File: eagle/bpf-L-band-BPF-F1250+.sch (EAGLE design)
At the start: 3 parts, among them U1 BPF-F1250+, X1 SMA-142-0701-801/806, X2 SMA-142-0701-801/806

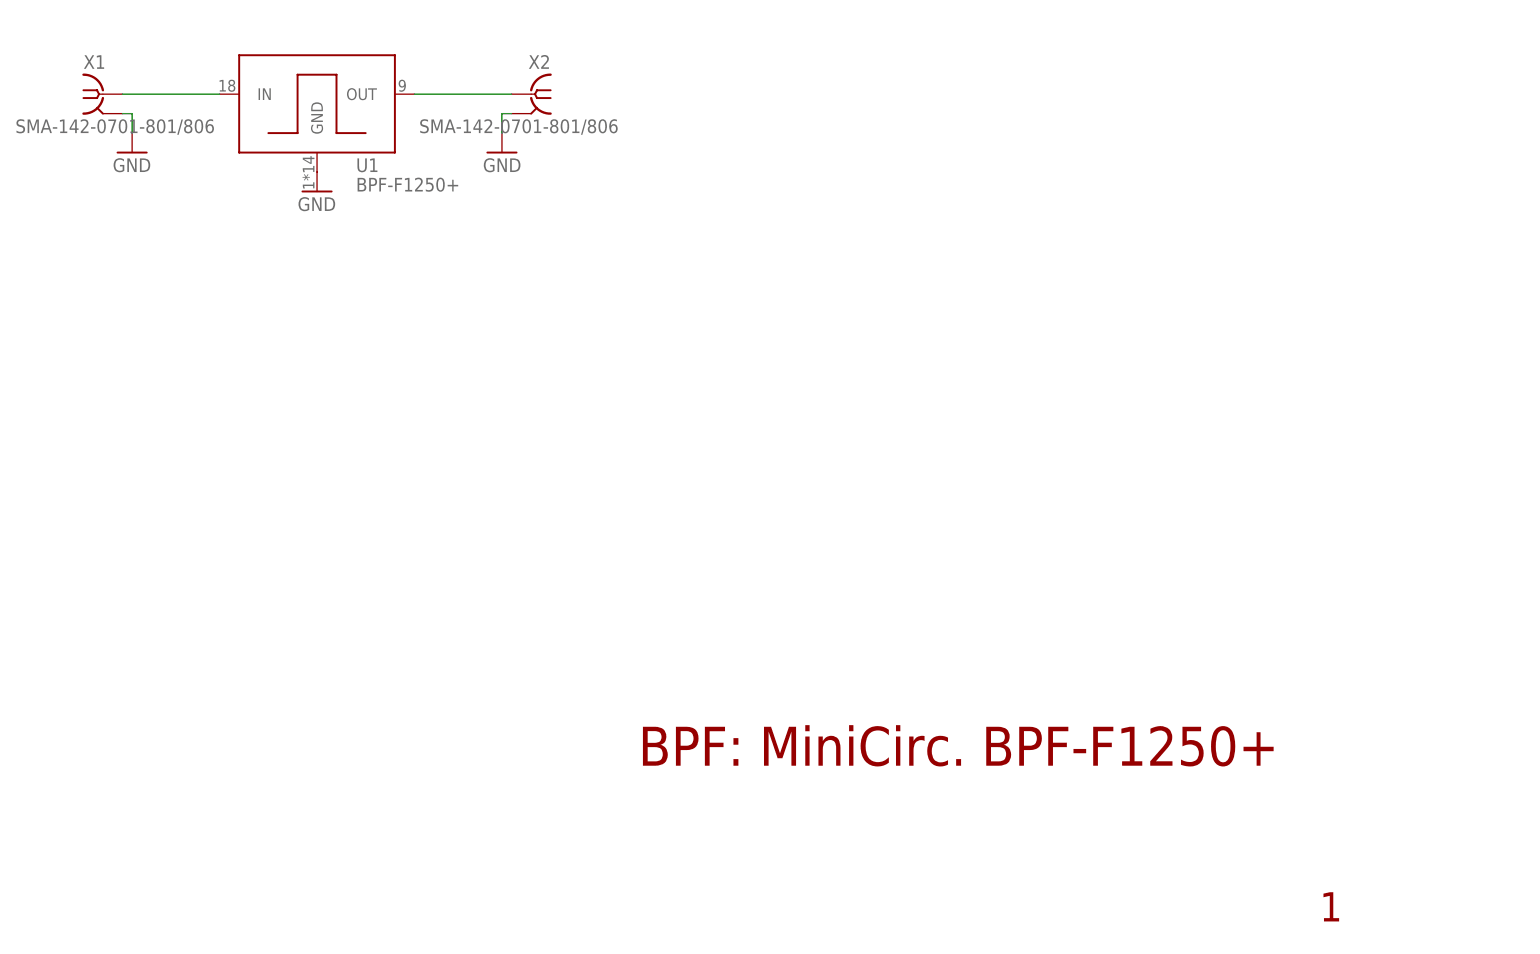
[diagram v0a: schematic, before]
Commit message: Add layout for BPF-F1250+
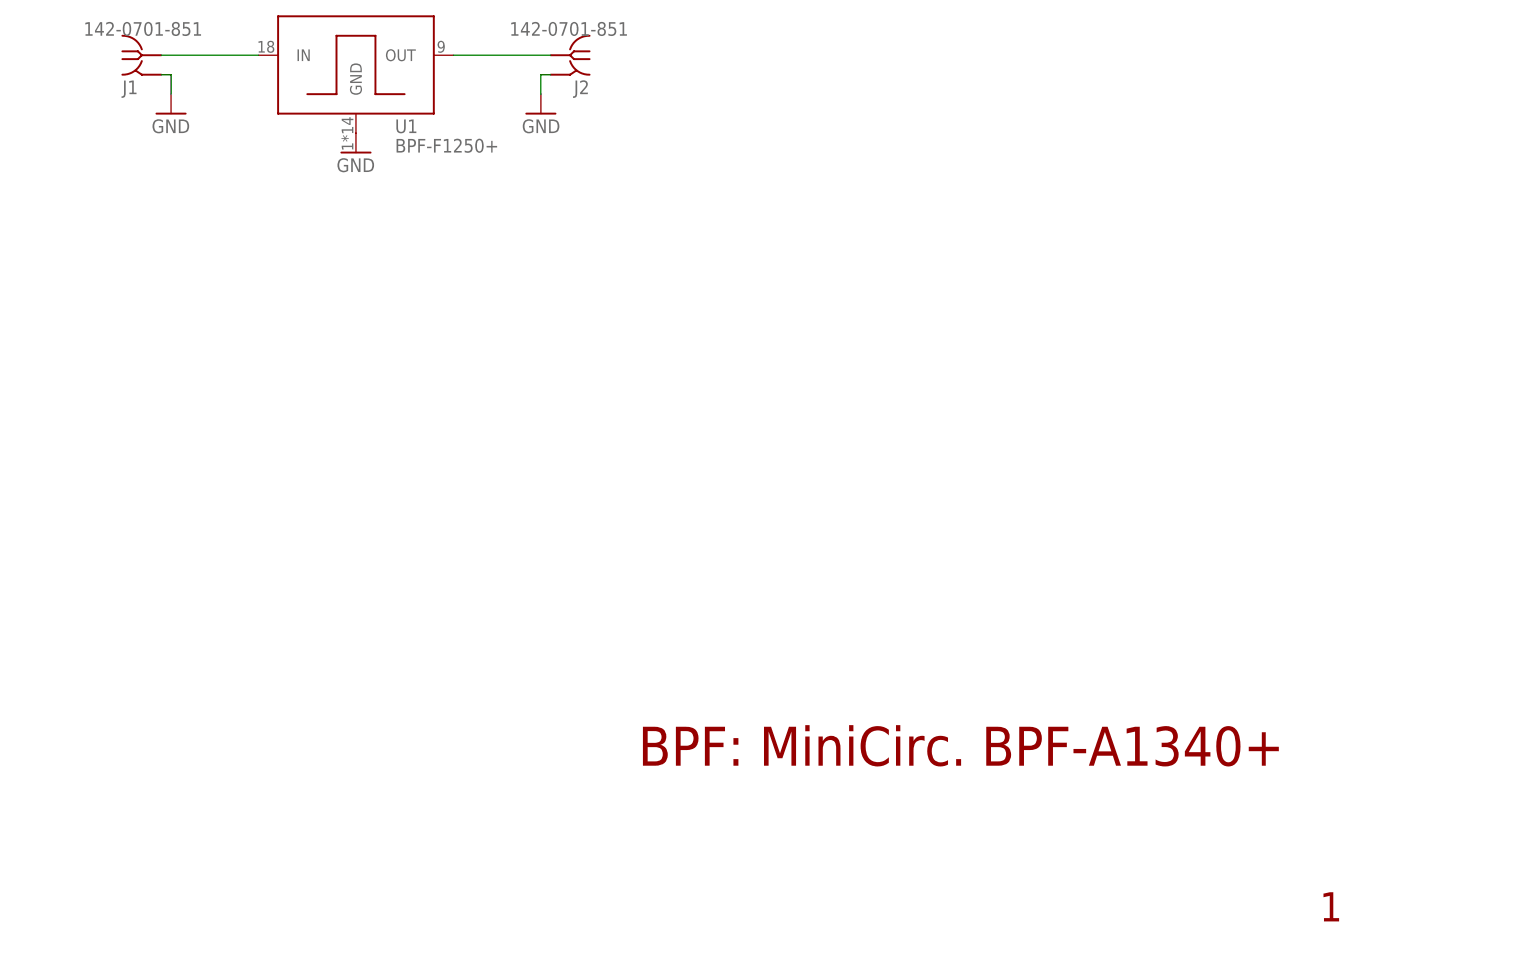
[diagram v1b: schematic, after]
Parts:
- removed X1, X2: SMA-142-0701-801/806, con-coax:SMA-142-0701-801/806
- added J1, J2: 142-0701-851, J-Cinch-142-0701-851-SMA-end-launch:142-0701-851
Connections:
- removed net N$83: U1.IN, X1.1
- removed net N$85: U1.OUT, X2.1
- new net RF-IN: J1.RF, U1.IN
- new net RF-OUT: J2.RF, U1.OUT
- net GND: now also J1.GND, J2.GND; no longer X1.2, X2.2
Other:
- note added: "BPF: MiniCirc. BPF-A1340+"
- note removed: "BPF: MiniCirc. BPF-F1250+"
- moved on the sheet: U1
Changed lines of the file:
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@@
 <class number="0" name="default" width="0" drill="0">
+</class>
+<class number="1" name="RF" width="0" drill="0">
+<clearance class="1" value="0.8"/>
 </class>
 </classes>
 <parts>
 <part name="FRAME2" library="frames" library_urn="urn:adsk.eagle:library:229" deviceset="FRAME_A_L" device=""/>
-<part name="X1" library="con-coax" library_urn="urn:adsk.eagle:library:133" deviceset="SMA-" device="142-0701-801/806" package3d_urn="urn:adsk.eagle:package:6214/1"/>
-<part name="GND93" library="supply1" library_urn="urn:adsk.eagle:library:371" deviceset="GND" device=""/>
-<part name="X2" library="con-coax" library_urn="urn:adsk.eagle:library:133" deviceset="SMA-" device="142-0701-801/806" package3d_urn="urn:adsk.eagle:package:6214/1"/>
-<part name="GND94" library="supply1" library_urn="urn:adsk.eagle:library:371" deviceset="GND" device=""/>
-<part name="GND95" library="supply1" library_urn="urn:adsk.eagle:library:371" deviceset="GND" device=""/>
+<part name="GND79" library="supply1" library_urn="urn:adsk.eagle:library:371" deviceset="GND" device=""/>
+<part name="GND91" library="supply1" library_urn="urn:adsk.eagle:library:371" deviceset="GND" device=""/>
+<part name="GND96" library="supply1" library_urn="urn:adsk.eagle:library:371" deviceset="GND" device=""/>
+<part name="J1" library="J-Cinch-142-0701-851-SMA-end-launch" deviceset="142-0701-851" device=""/>
+<part name="J2" library="J-Cinch-142-0701-851-SMA-end-launch" deviceset="142-0701-851" device=""/>
 <part name="U1" library="U-MiniCirc-BPF-F1250+-BPF" deviceset="BPF-F1250+" device=""/>
 </parts>
@@
 <sheet>
 <plain>
-<text x="176.53" y="26.67" size="5.08" layer="94">BPF: MiniCirc. BPF-F1250+</text>
+<text x="176.53" y="26.67" size="5.08" layer="94">BPF: MiniCirc. BPF-A1340+</text>
 <text x="265.43" y="6.35" size="3.81" layer="94">1</text>
 </plain>
@@
 <attribute name="DRAWING_NAME" x="190.5" y="19.05" size="2.54" layer="94"/>
 </instance>
-<instance part="X1" gate="G1" x="106.68" y="114.3" smashed="yes">
-<attribute name="VALUE" x="95.25" y="109.22" size="1.778" layer="96"/>
-<attribute name="NAME" x="104.14" y="117.602" size="1.778" layer="95"/>
+<instance part="GND79" gate="1" x="115.57" y="111.76" smashed="yes">
+<attribute name="VALUE" x="113.03" y="109.22" size="1.778" layer="96"/>
 </instance>
-<instance part="GND93" gate="1" x="110.49" y="106.68" smashed="yes">
-<attribute name="VALUE" x="107.95" y="104.14" size="1.778" layer="96"/>
+<instance part="GND91" gate="1" x="163.83" y="111.76" smashed="yes" rot="MR0">
+<attribute name="VALUE" x="166.37" y="109.22" size="1.778" layer="96" rot="MR0"/>
 </instance>
-<instance part="X2" gate="G1" x="162.56" y="114.3" smashed="yes" rot="MR0">
-<attribute name="VALUE" x="173.99" y="109.22" size="1.778" layer="96" rot="MR0"/>
-<attribute name="NAME" x="165.1" y="117.602" size="1.778" layer="95" rot="MR0"/>
+<instance part="GND96" gate="1" x="139.7" y="106.68" smashed="yes">
+<attribute name="VALUE" x="137.16" y="104.14" size="1.778" layer="96"/>
 </instance>
-<instance part="GND94" gate="1" x="158.75" y="106.68" smashed="yes" rot="MR0">
-<attribute name="VALUE" x="161.29" y="104.14" size="1.778" layer="96" rot="MR0"/>
+<instance part="J1" gate="G$1" x="111.76" y="119.38" smashed="yes">
+<attribute name="NAME" x="109.22" y="114.3" size="1.778" layer="95"/>
+<attribute name="VALUE" x="104.14" y="121.92" size="1.778" layer="96"/>
 </instance>
-<instance part="GND95" gate="1" x="134.62" y="101.6" smashed="yes">
-<attribute name="VALUE" x="132.08" y="99.06" size="1.778" layer="96"/>
+<instance part="J2" gate="G$1" x="167.64" y="119.38" smashed="yes" rot="MR0">
+<attribute name="NAME" x="170.18" y="114.3" size="1.778" layer="95" rot="MR0"/>
+<attribute name="VALUE" x="175.26" y="121.92" size="1.778" layer="96" rot="MR0"/>
 </instance>
-<instance part="U1" gate="G$1" x="134.62" y="111.76" smashed="yes">
-<attribute name="NAME" x="139.7" y="104.14" size="1.778" layer="95"/>
-<attribute name="VALUE" x="139.7" y="101.6" size="1.778" layer="96"/>
+<instance part="U1" gate="G$1" x="139.7" y="116.84" smashed="yes">
+<attribute name="NAME" x="144.78" y="109.22" size="1.778" layer="95"/>
+<attribute name="VALUE" x="144.78" y="106.68" size="1.778" layer="96"/>
 </instance>
 </instances>
@@
 <net name="GND" class="0">
 <segment>
-<pinref part="X1" gate="G1" pin="2"/>
-<pinref part="GND93" gate="1" pin="GND"/>
-<wire x1="109.22" y1="111.76" x2="110.49" y2="111.76" width="0.1524" layer="91"/>
-<wire x1="110.49" y1="111.76" x2="110.49" y2="109.22" width="0.1524" layer="91"/>
+<pinref part="GND79" gate="1" pin="GND"/>
+<wire x1="114.3" y1="116.84" x2="115.57" y2="116.84" width="0.1524" layer="91"/>
+<wire x1="115.57" y1="116.84" x2="115.57" y2="114.3" width="0.1524" layer="91"/>
+<pinref part="J1" gate="G$1" pin="GND"/>
 </segment>
 <segment>
-<pinref part="X2" gate="G1" pin="2"/>
-<pinref part="GND94" gate="1" pin="GND"/>
-<wire x1="160.02" y1="111.76" x2="158.75" y2="111.76" width="0.1524" layer="91"/>
-<wire x1="158.75" y1="111.76" x2="158.75" y2="109.22" width="0.1524" layer="91"/>
+<pinref part="GND91" gate="1" pin="GND"/>
+<wire x1="165.1" y1="116.84" x2="163.83" y2="116.84" width="0.1524" layer="91"/>
+<wire x1="163.83" y1="116.84" x2="163.83" y2="114.3" width="0.1524" layer="91"/>
+<pinref part="J2" gate="G$1" pin="GND"/>
 </segment>
 <segment>
-<pinref part="GND95" gate="1" pin="GND"/>
+<pinref part="GND96" gate="1" pin="GND"/>
 <pinref part="U1" gate="G$1" pin="GND"/>
 </segment>
 </net>
-<net name="N$83" class="0">
+<net name="RF-IN" class="1">
 <segment>
-<pinref part="X1" gate="G1" pin="1"/>
-<wire x1="109.22" y1="114.3" x2="121.92" y2="114.3" width="0.1524" layer="91"/>
+<wire x1="114.3" y1="119.38" x2="127" y2="119.38" width="0.1524" layer="91"/>
+<pinref part="J1" gate="G$1" pin="RF"/>
 <pinref part="U1" gate="G$1" pin="IN"/>
 </segment>
 </net>
-<net name="N$85" class="0">
+<net name="RF-OUT" class="1">
 <segment>
-<pinref part="X2" gate="G1" pin="1"/>
-<wire x1="160.02" y1="114.3" x2="147.32" y2="114.3" width="0.1524" layer="91"/>
+<wire x1="165.1" y1="119.38" x2="152.4" y2="119.38" width="0.1524" layer="91"/>
+<pinref part="J2" gate="G$1" pin="RF"/>
 <pinref part="U1" gate="G$1" pin="OUT"/>
 </segment>
@@
 will not be understood (or retained) with this version.
 </note>
-<note version="8.3" severity="warning">
-Since Version 8.3, EAGLE supports the association of 3D packages
-with devices in libraries, schematics, and board files. Those 3D
-packages will not be understood (or retained) with this version.
-</note>
 </compatibility>
